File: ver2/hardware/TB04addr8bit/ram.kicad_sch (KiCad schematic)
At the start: 6 parts, among them U1101 6116, U1102 74HC244, U1103 74HC244

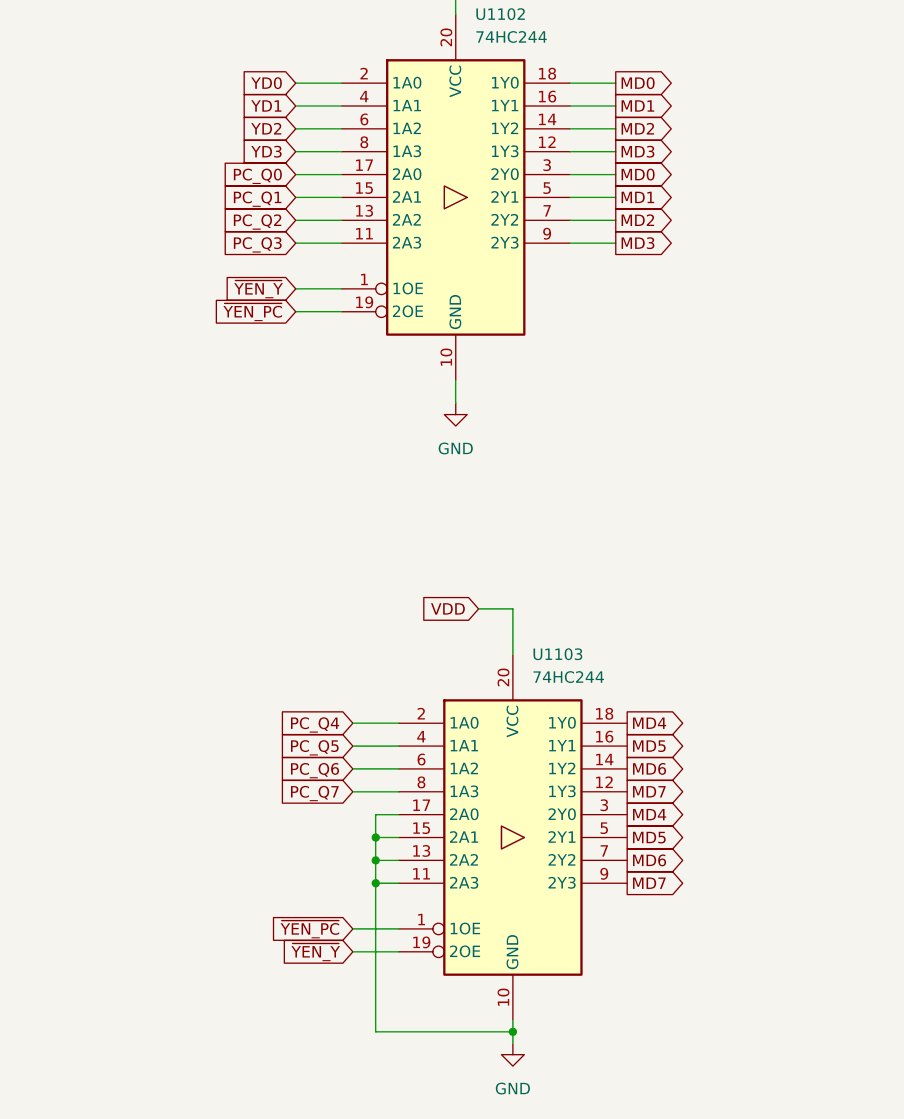
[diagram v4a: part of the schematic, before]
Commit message: ver2: Yドライバ/PCドライバを1チップ1機能に整理
- ram: 74HC244×2を組み替え。U1102=Yドライバ専用(YD0-3→MD0-3、
  bank2はGND→MD4-7で上位0埋め、OE2本とも~YEN_Y)、U1103=PCドライバ
  専用(PC_Q0-7→MD0-7、OE2本とも~YEN_PC)。接続の集合は変更前と完全
  一致で機能等価。PCの8bitが1チップに揃いビット間スキューが揃う
- inPut: U1001のbank2イネーブル(pin19)をVDDから~OE_iAddrへ。
  出力2Y0-3はno_connectのままなので効果は未発現
- addrMUX/sp: 未使用出力のスタブ位置調整のみ(接続変更なし)

Co-Authored-By: Claude Opus 5 <noreply@anthropic.com>
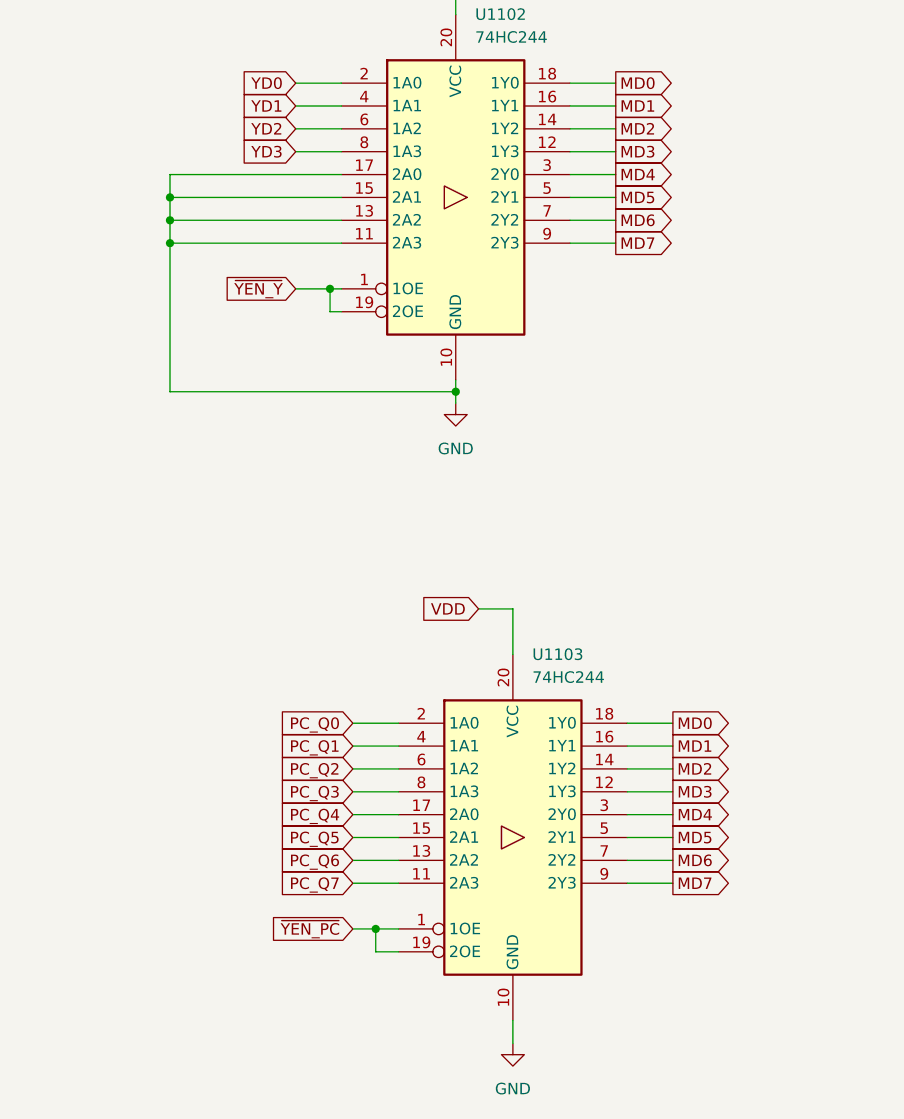
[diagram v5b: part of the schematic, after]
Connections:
- net GND: now also U1102.11 (2A3), U1102.13 (2A2), U1102.15 (2A1), U1102.17 (2A0); no longer U1103.11 (2A3), U1103.13 (2A2), U1103.15 (2A1), U1103.17 (2A0)
- net MD0: now also U1103.18 (1Y0); no longer U1102.3 (2Y0)
- net MD1: now also U1103.16 (1Y1); no longer U1102.5 (2Y1)
- net MD2: now also U1103.14 (1Y2); no longer U1102.7 (2Y2)
- net MD3: now also U1103.12 (1Y3); no longer U1102.9 (2Y3)
- net MD4: now also U1102.3 (2Y0); no longer U1103.18 (1Y0)
- net MD5: now also U1102.5 (2Y1); no longer U1103.16 (1Y1)
- net MD6: now also U1102.7 (2Y2); no longer U1103.14 (1Y2)
- net MD7: now also U1102.9 (2Y3); no longer U1103.12 (1Y3)
- net PC_Q0: now also U1103.2 (1A0); no longer U1102.17 (2A0)
- net PC_Q1: now also U1103.4 (1A1); no longer U1102.15 (2A1)
- net PC_Q2: now also U1103.6 (1A2); no longer U1102.13 (2A2)
- net PC_Q3: now also U1103.8 (1A3); no longer U1102.11 (2A3)
- net PC_Q4: now also U1103.17 (2A0); no longer U1103.2 (1A0)
- net PC_Q5: now also U1103.15 (2A1); no longer U1103.4 (1A1)
- net PC_Q6: now also U1103.13 (2A2); no longer U1103.6 (1A2)
- net PC_Q7: now also U1103.11 (2A3); no longer U1103.8 (1A3)
- net ~{YEN_PC}: now also U1103.19 (2OE); no longer U1102.19 (2OE)
- net ~{YEN_Y}: now also U1102.19 (2OE); no longer U1103.19 (2OE)
